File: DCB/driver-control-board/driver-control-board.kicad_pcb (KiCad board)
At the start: 2 copper layers, 92.7 x 59.2 mm, 34 parts, among them J1 Conn_01x05, J2 Conn_01x14, J3 Conn_01x08, J4 Conn_01x23, U1 STM32F413CGUx, U2 LD1117S33TR_SOT223, U3 R-78B5.0-2.0, U4 MCP2551-I-SN, Y1 Crystal

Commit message: adding mounting holes
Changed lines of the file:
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@@
     (property "Sheetname" "")
     (attr smd)
-    (fp_text reference "R7" (at 0 -1.43 90) (layer "F.SilkS")
+    (fp_text reference "R7" (at -0.1505 1.6275 90) (layer "F.SilkS")
       (effects (font (size 1 1) (thickness 0.15)))
     )
@@
     (property "Sheetname" "")
     (attr smd)
-    (fp_text reference "C14" (at 0 -1.43 90) (layer "F.SilkS")
+    (fp_text reference "C14" (at 0 -1.6275 90) (layer "F.SilkS")
       (effects (font (size 1 1) (thickness 0.15)))
     )
@@
     (property "Sheetname" "")
     (attr smd)
-    (fp_text reference "U4" (at 0 -3.4 90) (layer "F.SilkS")
-      (effects (font (size 1 1) (thickness 0.15)))
-    )
+    (fp_text reference "U4" (at 0.127 3.5795 90) (layer "F.SilkS")
+      (effects (font (size 1 1) (thickness 0.15)))
+    )

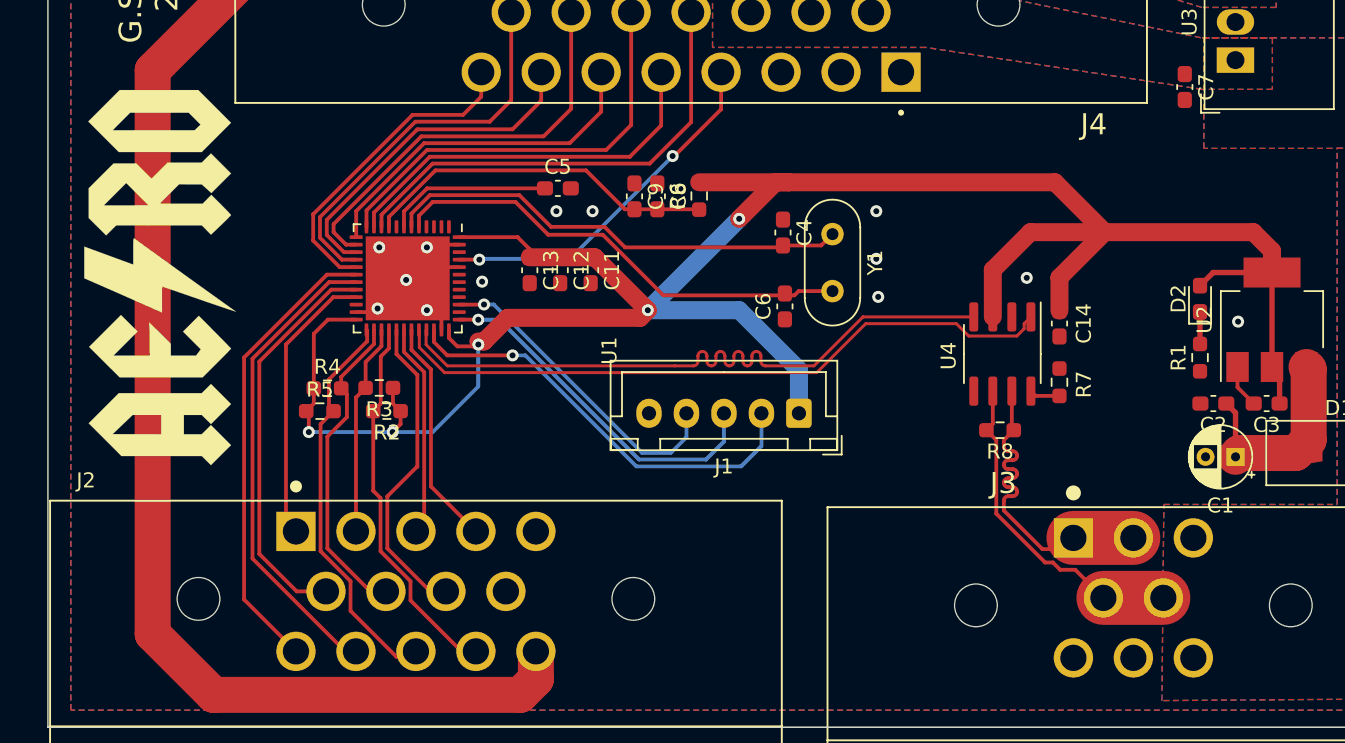
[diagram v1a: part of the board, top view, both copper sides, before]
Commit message: updating filtering cap layout
Kay suggested layout changes. Moved caps around
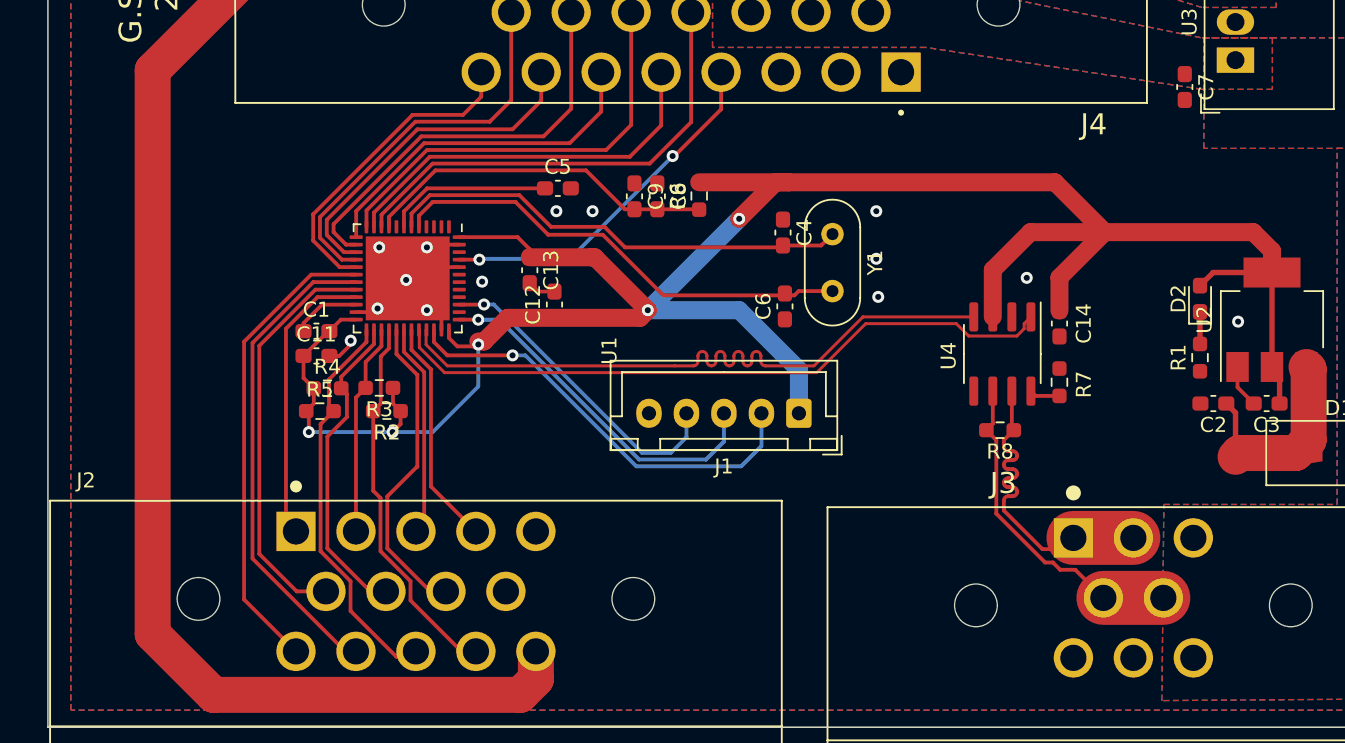
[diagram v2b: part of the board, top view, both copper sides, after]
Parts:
- removed G***: LOGO, AERO_Footprints:AERO_Logo_25x10mm
- C1: value CP1 -> 4.7u; footprint Capacitor_THT:CP_Radial_D4.0mm_P2.00mm -> Capacitor_SMD:C_0603_1608Metric_Pad1.08x0.95mm_HandSolder
- C10, C3: value C -> 10u
- C2, C7: value C -> .1u
- R1: value R -> 220
- moved C1 61.9 mm to (113.4, 137.9), turned to 0 degrees
- moved C11 19.2 mm to (113.4, 139.6), turned to 0 degrees
- moved C12 2.32 mm to (129.3, 136.1), turned to 90 degrees
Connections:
- C1 pad 1: Net-(C1-Pad1) -> Net-(U1-Pad22)
- C1 pad 2: GND -> +3V3
- C2 pad 1: Net-(C1-Pad1) -> Net-(C2-Pad1)
- D1 pad 1: Net-(C1-Pad1) -> Net-(C2-Pad1)
- U1 pad 22: unconnected-(U1-Pad22) -> Net-(U1-Pad22)
- U2 pad 3: Net-(C1-Pad1) -> Net-(C2-Pad1)
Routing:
- net Net-(C2-Pad1): track 0.00 -> 14.1 mm
- net Net-(C1-Pad1): track 14.1 -> 0.00 mm
- net Net-(U1-Pad22): track 0.00 -> 4.56 mm
- net GND: track 19.7 -> 23.6 mm, vias 13 -> 14
- net /IMD_LED: track 26.8 -> 27.4 mm
- net /POT_BRAKE: track 31.8 -> 32.4 mm
- net /POT_REGEN: track 30.8 -> 31.4 mm
- net /RTD_LED: track 18.7 -> 19.4 mm
- net /CAN_P: track 23.4 -> 22.8 mm
- net A13_SWDIO: track 29.4 -> 28.8 mm

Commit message: DRC and Labeling Complete
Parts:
- added G***: LOGO, AERO_Footprints:AERO_Logo_25x10mm, F.Cu at (99.9, 97.8)
- moved C4 37.9 mm to (142.6, 93.5)
- moved D1 37.9 mm to (179.7, 108.2)
- moved R8 37.9 mm to (157.1, 106.7)
- moved C7 37.9 mm to (169.4, 83.8)
- moved U4 37.9 mm to (157.2, 101.6)
- moved C1 37.9 mm to (111.5, 100.1)
- moved C10 37.9 mm to (175.6, 72.4)
- moved C11 37.9 mm to (111.5, 101.8)
- moved C12 37.9 mm to (127.4, 98.3)
- moved C13 37.9 mm to (125.7, 96.1)
- moved C8 37.9 mm to (134.2, 91.1)
- moved C9 37.9 mm to (132.7, 91.1)
- moved D2 37.9 mm to (170.4, 98.0)
- moved J1 37.9 mm to (143.7, 105.6)
- moved J2 37.9 mm to (118.1, 117.5)
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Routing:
- net Net-(C2-Pad1): track 14.1 -> 12.1 mm

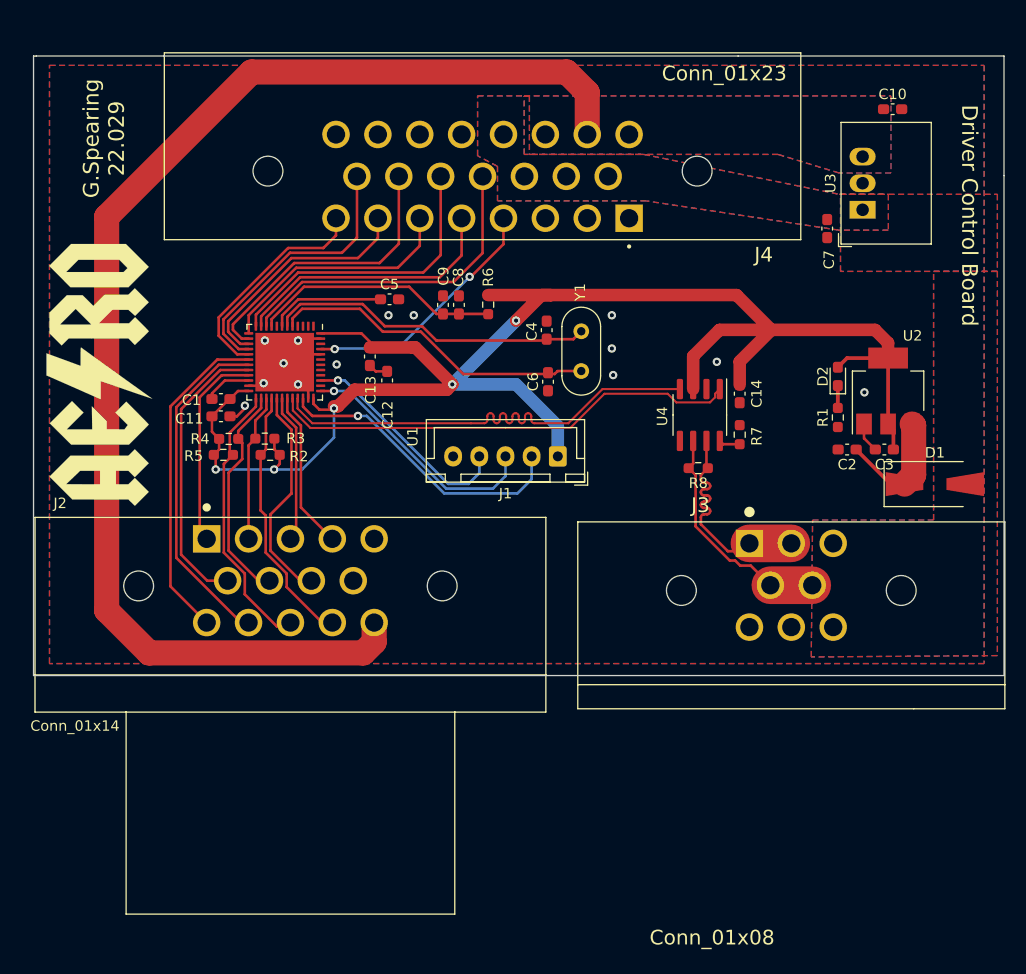
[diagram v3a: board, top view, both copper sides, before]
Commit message: layout and labeling update
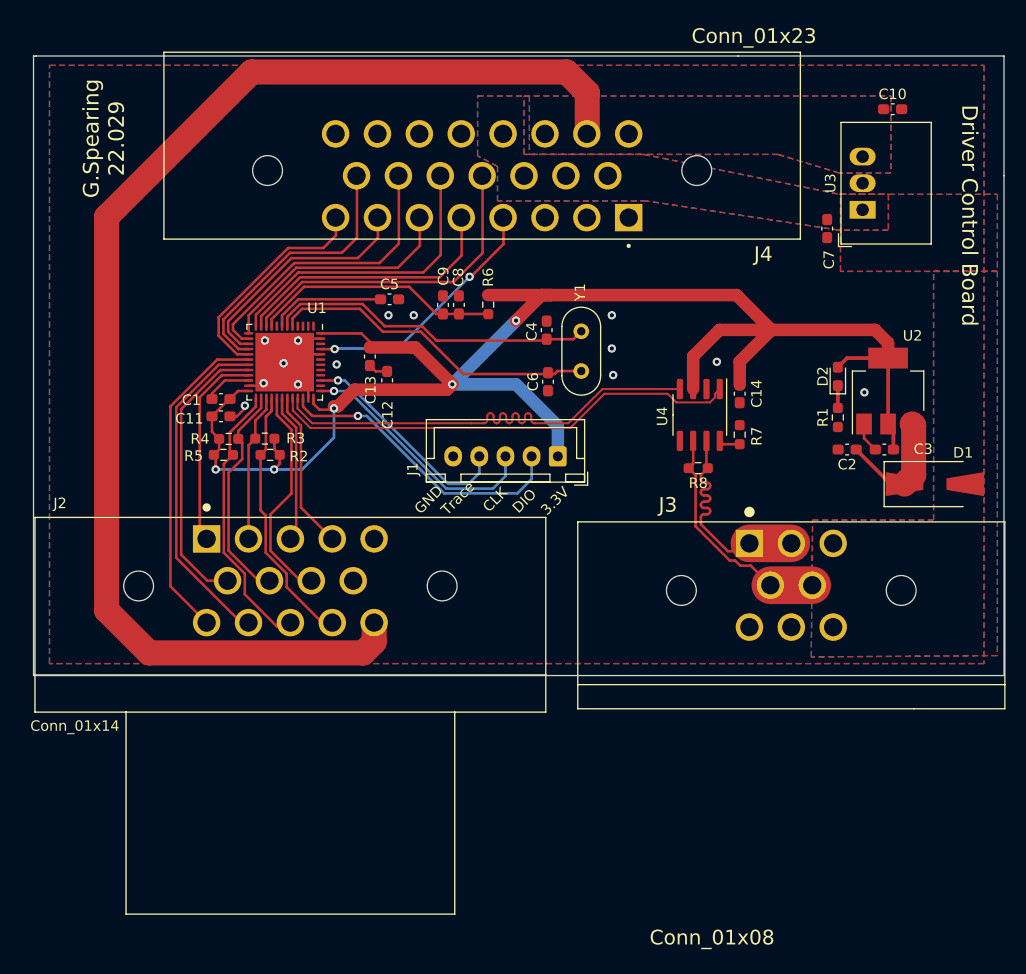
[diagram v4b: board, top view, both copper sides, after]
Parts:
- removed G***: LOGO, AERO_Footprints:AERO_Logo_25x10mm
- moved J4 0.07 mm to (150.4, 82.8)
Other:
- board text added: "3.3V"
- board text added: "CLK"
- board text added: "DIO"
- board text added: "GND"
- board text added: "Trace"

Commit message: working on layout
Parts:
- removed R2, R3, R4, R5: 10k, Resistor_SMD:R_0603_1608Metric_Pad0.98x0.95mm_HandSolder
- added J5: Conn_02x10_Counter_Clockwise, Connector_PinHeader_2.54mm:PinHeader_2x10_P2.54mm_Horizontal, F.Cu at (152.1, 95.3)
- added J6: Conn_01x14, AERO_Footprints:TE_1-776266-1_14pin_Horizontal, F.Cu at (141.0, 128.4)
- added RN1: R_Pack04, Resistor_SMD:R_Array_Convex_4x1206, F.Cu at (76.3, 115.1)
- moved C14 63.4 mm to (101.1, 120.4), turned to 0 degrees
- moved R7 58.4 mm to (105.2, 120.4), turned to 0 degrees
- moved U4 56.2 mm to (103.1, 116.8), turned to 0 degrees
- moved C10 56.1 mm to (123.4, 93.0), turned to 90 degrees
- moved C12 55.7 mm to (72.9, 110.2), turned to 180 degrees
- moved C3 53.0 mm to (122.2, 110.7)
- moved D1 50.4 mm to (129.3, 106.9), turned to 180 degrees
- moved C8 50.3 mm to (84.3, 97.8), turned to 90 degrees
- moved U3 49.8 mm to (126.6, 100.5)
- moved C7 49.7 mm to (123.2, 102.1)
- moved D2 49.5 mm to (122.2, 109.0), turned to 0 degrees
- moved R6 49.3 mm to (88.1, 97.8)
- moved R8 49.2 mm to (109.0, 116.8), turned to -90 degrees
- moved R1 48.6 mm to (122.2, 107.4), turned to 180 degrees
- moved J4 48.5 mm to (102.4, 89.4)
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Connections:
- J3 pad 1: /CAN_P -> +12V
- J3 pad 2: /CAN_P -> /CAN_N
- J3 pad 3: +12V -> /CAN_P
- J3 pad 5: /CAN_N -> /CAN_P
- J3 pad 6: GND -> +12V
- J3 pad 8: +12V -> GND
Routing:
- net +12V: track 0.00 -> 112.0 mm
- net +5V: track 123.6 -> 38.0 mm
- net /CAN_N: track 22.1 -> 82.4 mm
- net /CAN_P: track 22.8 -> 80.3 mm
- net /12V_OUT: track 0.00 -> 56.5 mm
- net /5V_OUT: track 0.00 -> 48.5 mm
- net /Heater: track 0.00 -> 40.6 mm
- net /DISP-: track 0.00 -> 37.5 mm
- net /DISP+: track 0.00 -> 34.9 mm
- net /USB_D-: track 0.00 -> 31.5 mm
- net /USB_D+: track 0.00 -> 29.9 mm
- net /USB_GND: track 0.00 -> 28.3 mm
- net /USB_PWR: track 0.00 -> 27.6 mm
- net /CURRENT_GND: track 0.00 -> 22.8 mm
- net /CURRENT_2: track 0.00 -> 19.2 mm
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- removed copper zone on B.Cu, net +12V
- removed copper zone on F.Cu, net +12V
- removed copper zone on B.Cu, net +5V
- removed copper zone on F.Cu, net +5V
- removed copper zone on B.Cu, net GND
- removed copper zone on F.Cu, net GND
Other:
- board size 92.7 x 59.2 mm -> 95.5 x 61 mm
- board text removed: "3.3V"
- board text removed: "CLK"
- board text removed: "DIO"
- board text removed: "Driver Control Board"
- board text removed: "G.Spearing 22.029"
- board text removed: "GND"
- board text removed: "Trace"
